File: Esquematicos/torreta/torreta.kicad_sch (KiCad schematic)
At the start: 5 parts, among them U1 ATmega328-P

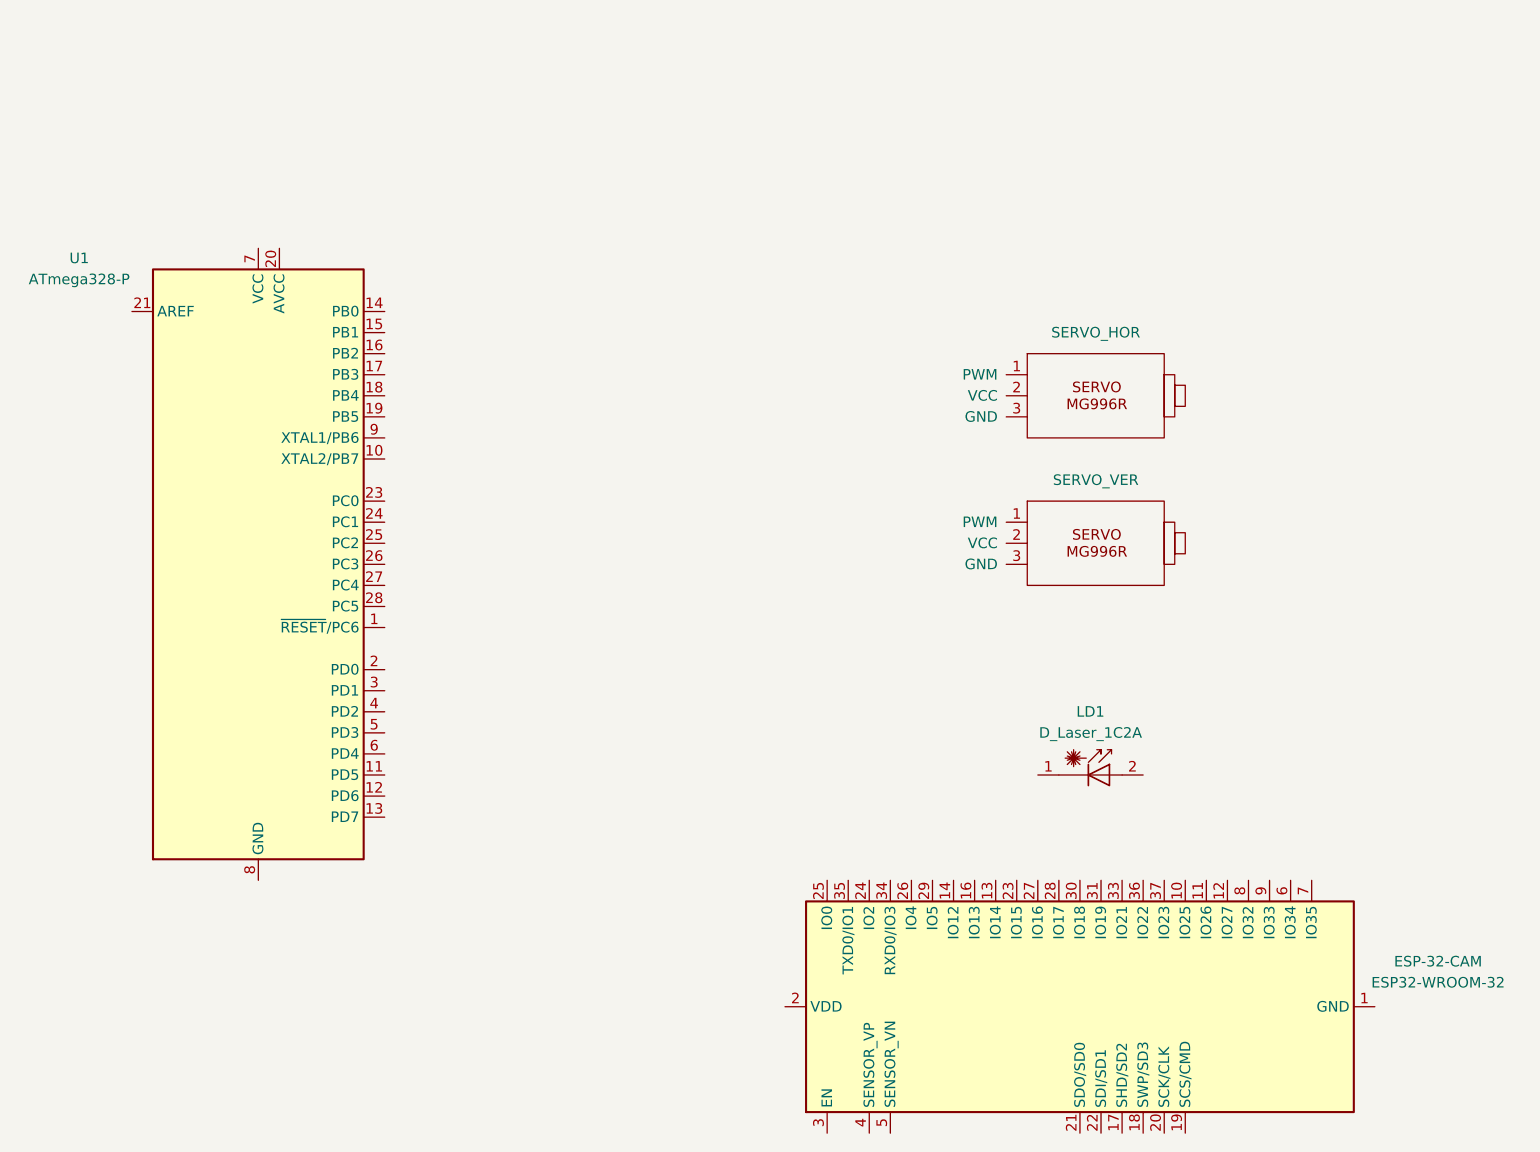
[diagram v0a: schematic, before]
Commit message: Avanzar esquematico. Completo pero le faltan conexiones a la PC
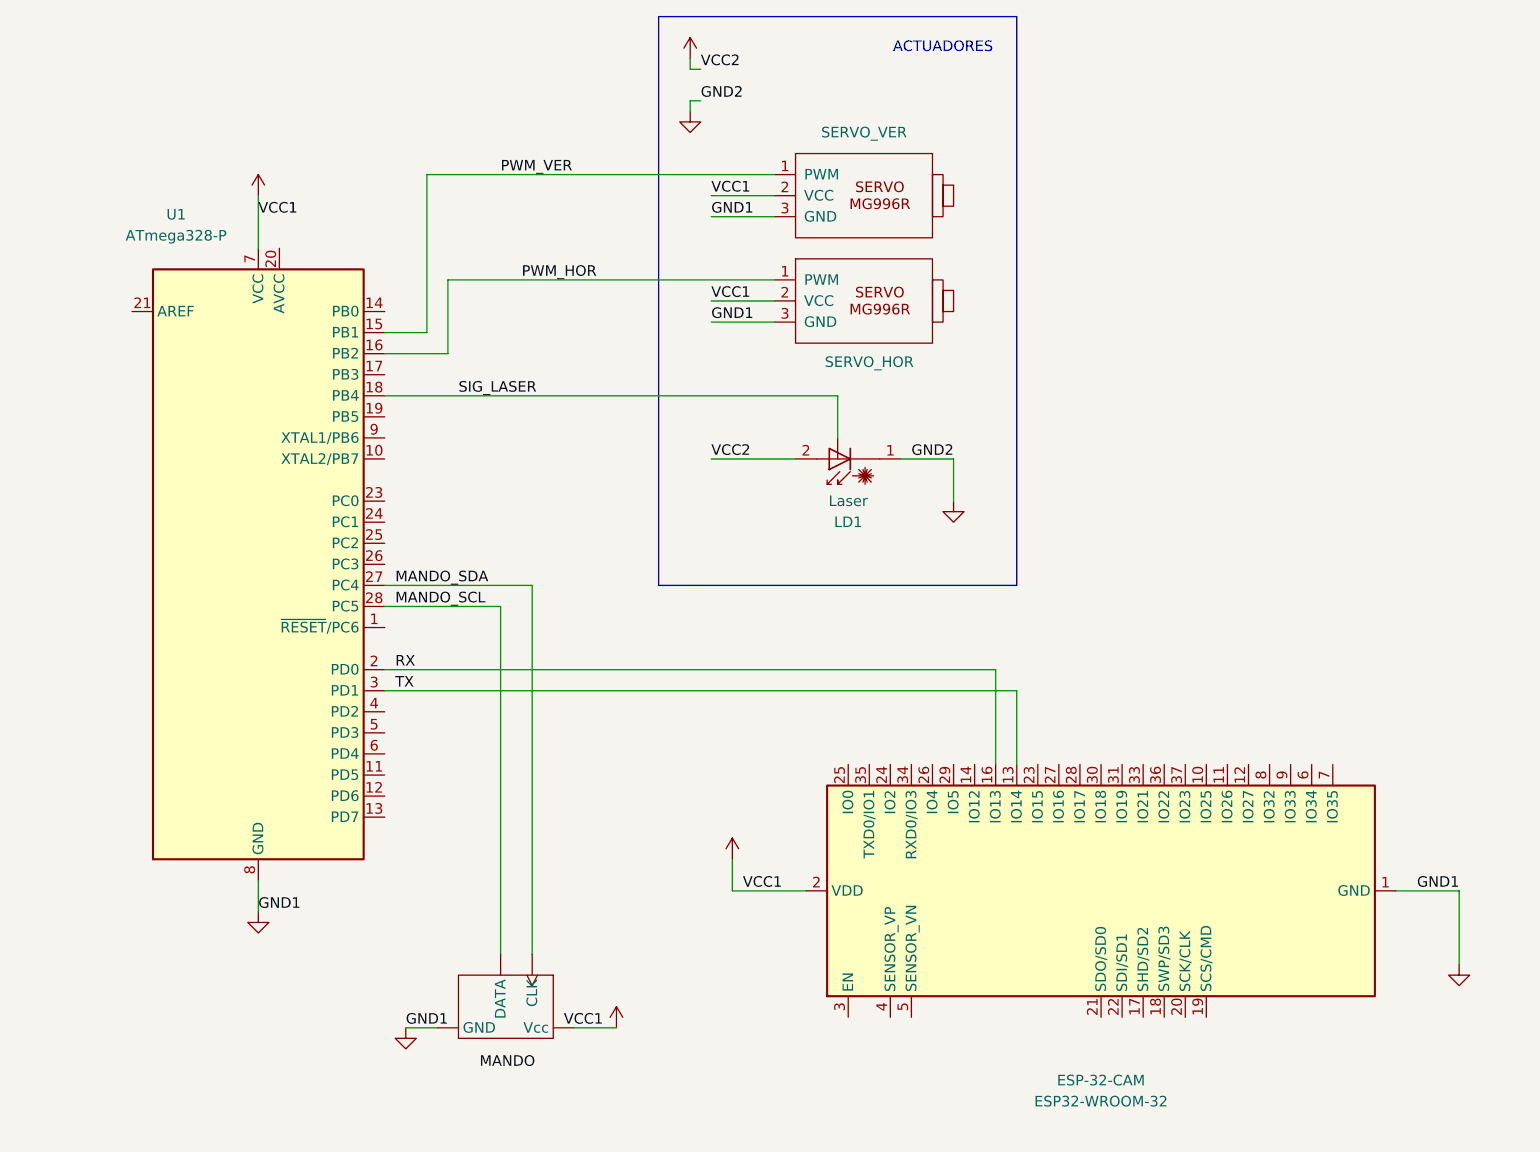
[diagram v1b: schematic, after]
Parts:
- added U2: (no value), symbol Torreta:Nunchuck
- LD1: value D_Laser_1C2A -> Laser
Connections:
- net PWM_HOR: now reaches SERVO_HOR.1 (PWM)
- net PWM_HOR: now also U1.16 (PB2)
- net VCC: now reaches SERVO_HOR.2 (VCC)
- net VCC: now also ESP-32-CAM.2 (VDD), LD1.2 (A), SERVO_VER.2 (VCC), U1.7 (VCC), U2. (GND)
- net GND: now reaches SERVO_HOR.3 (GND)
- net GND: now also ESP-32-CAM.1 (GND), ESP-32-CAM.15 (GND), ESP-32-CAM.38 (GND), ESP-32-CAM.39 (GND), LD1.1 (K), SERVO_VER.3 (GND), U1.22 (GND), U1.8 (GND), U2. (GND)
- net PWM_VER: now reaches U1.15 (PB1)
- net PWM_VER: now also SERVO_VER.1 (PWM)
- net SIG_LASER: now reaches U1.18 (PB4)
- net SIG_LASER: now also LD1. (Sig)
- net RX: now reaches U1.2 (PD0)
- net RX: now also ESP-32-CAM.16 (IO13)
- net MANDO_SDA: now reaches U1.27 (PC4)
- net MANDO_SDA: now also U2. (GND)
- net MANDO_SCL: now reaches U1.28 (PC5)
- net MANDO_SCL: now also U2. (GND)
- net TX: now reaches U1.3 (PD1)
- net TX: now also ESP-32-CAM.13 (IO14)
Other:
- note added: "ACTUADORES"
- moved on the sheet: ESP-32-CAM, SERVO_HOR, SERVO_VER
